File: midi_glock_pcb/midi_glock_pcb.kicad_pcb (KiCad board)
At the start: 2 copper layers, 7 parts, among them U11 ESP32-WROVER-E-N4R8, U12 DRV8860_PWPR, U13 DRV8860_PWPR, U14 DRV8860_PWPR, U15 DRV8860_PWPR, U6 TPS54302, U9 AMS1117-3.3

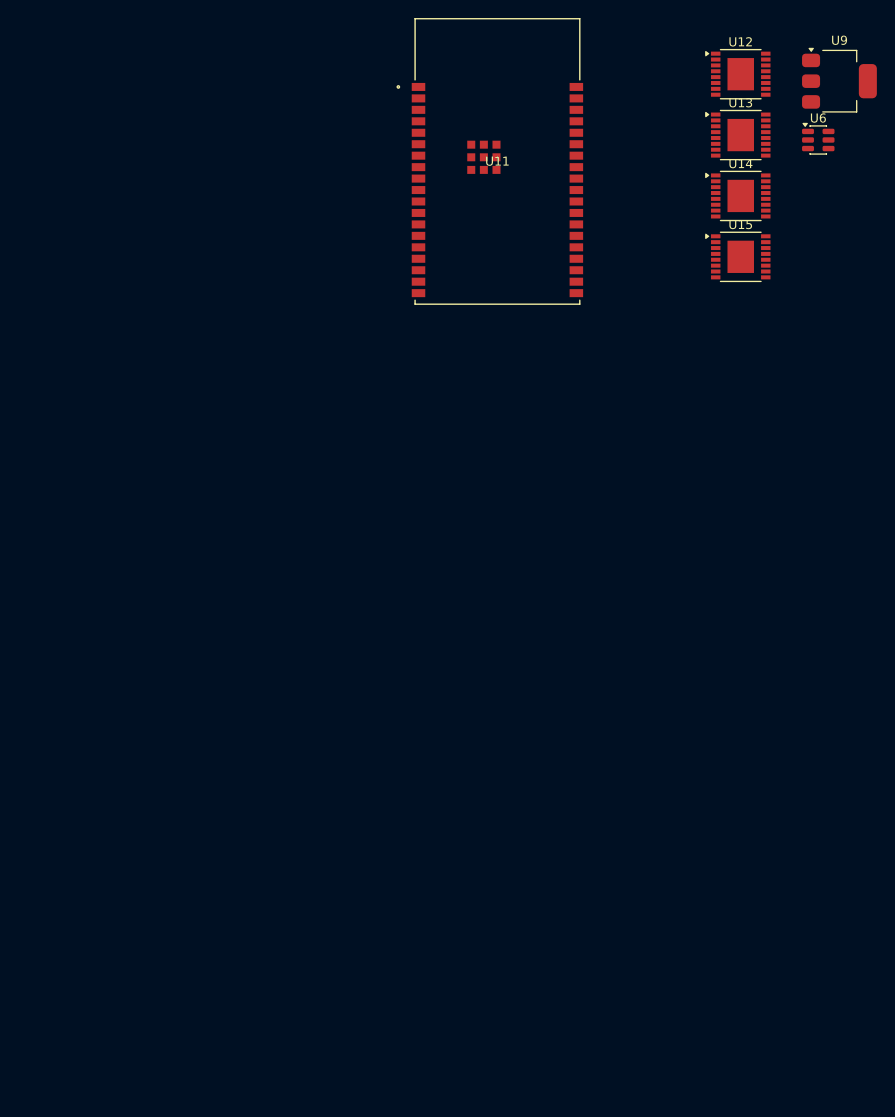
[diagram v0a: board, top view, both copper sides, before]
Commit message: pcb almost complete
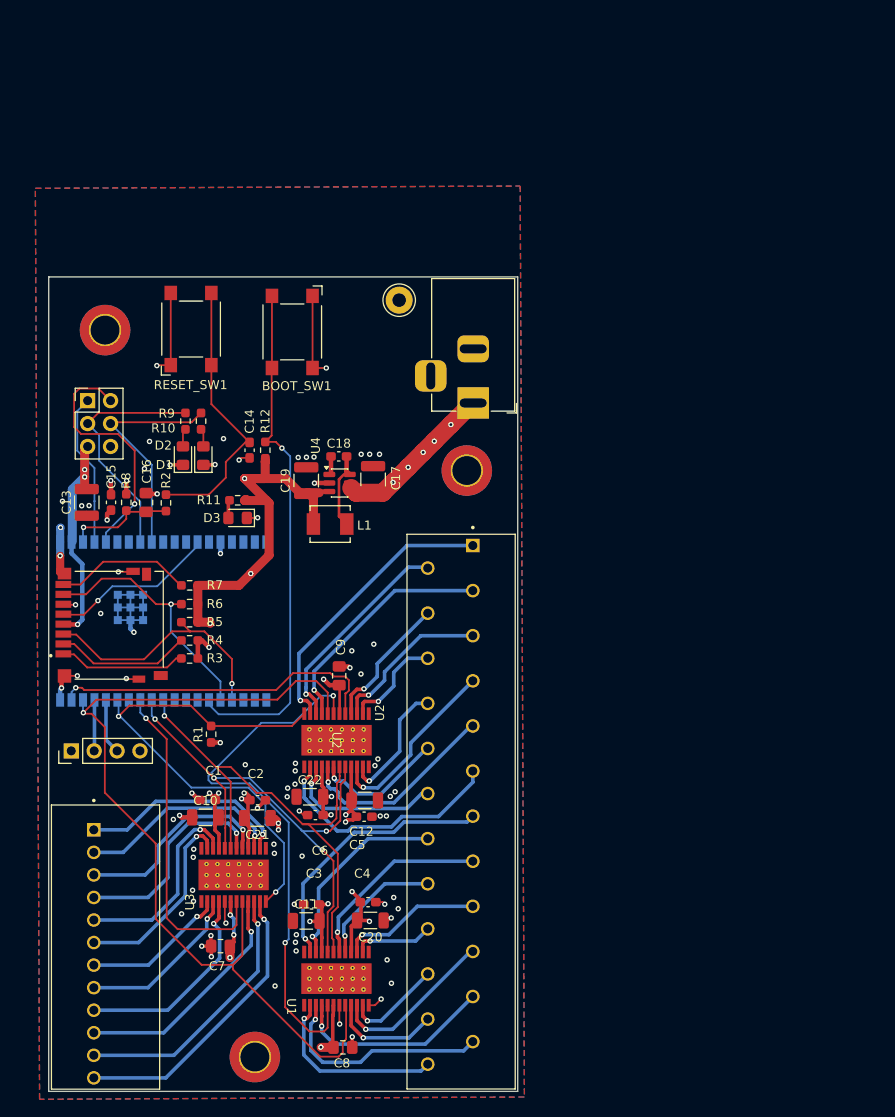
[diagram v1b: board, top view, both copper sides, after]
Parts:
- removed U12, U13, U14, U15: DRV8860_PWPR, Package_SO:TSSOP-16-1EP_4.4x5mm_P0.65mm
- removed U6: TPS54302, Package_TO_SOT_SMD:SOT-23-6
- removed U9: AMS1117-3.3, Package_TO_SOT_SMD:SOT-223-3_TabPin2
- added BOOT_SW1: SW_Push, Button_Switch_SMD:SW_SPST_Omron_B3FS-100xP, F.Cu at (75.0, 70.8)
- added C1: 0.1uF, Capacitor_SMD:C_0603_1608Metric_Pad1.08x0.95mm_HandSolder, F.Cu at (65.6, 122.7)
- added C10: 10uF, Capacitor_SMD:C_1206_3216Metric, F.Cu at (65.4, 124.6)
- added C11: 10uF, Capacitor_SMD:C_1206_3216Metric, F.Cu at (76.5, 136.1)
- added C12: 10uF, Capacitor_SMD:C_1206_3216Metric, F.Cu at (83.0, 122.7)
- added C13: 22uF, Capacitor_SMD:C_1210_3225Metric, F.Cu at (52.2, 89.7)
- added C14: 0.1uF, Capacitor_SMD:C_0603_1608Metric_Pad1.08x0.95mm_HandSolder, F.Cu at (70.3, 83.9)
- added C15: 0.1uF, Capacitor_SMD:C_0603_1608Metric_Pad1.08x0.95mm_HandSolder, F.Cu at (54.9, 89.7)
- added C16: 4.7uF, Capacitor_SMD:C_0805_2012Metric_Pad1.18x1.45mm_HandSolder, F.Cu at (58.8, 89.7)
- added C17: 22uf, Capacitor_SMD:C_1210_3225Metric, F.Cu at (84.0, 87.2)
- added C18: 100nf, Capacitor_SMD:C_0603_1608Metric_Pad1.08x0.95mm_HandSolder, F.Cu at (80.2, 84.6)
- added C19: 22uf, Capacitor_SMD:C_1210_3225Metric, F.Cu at (76.5, 87.3)
- added C2: 0.1uF, Capacitor_SMD:C_0603_1608Metric_Pad1.08x0.95mm_HandSolder, F.Cu at (71.2, 122.7)
- added C20: 10uF, Capacitor_SMD:C_1206_3216Metric, F.Cu at (83.7, 136.1)
- added C21: 10uF, Capacitor_SMD:C_1206_3216Metric, F.Cu at (71.1, 124.7)
- added C22: 10uF, Capacitor_SMD:C_1206_3216Metric, F.Cu at (77.0, 122.3)
- added C3: 0.1uF, Capacitor_SMD:C_0603_1608Metric_Pad1.08x0.95mm_HandSolder, F.Cu at (77.1, 134.3)
- added C4: 0.1uF, Capacitor_SMD:C_0603_1608Metric_Pad1.08x0.95mm_HandSolder, F.Cu at (83.4, 134.0)
- added C5: 0.1uF, Capacitor_SMD:C_0603_1608Metric_Pad1.08x0.95mm_HandSolder, F.Cu at (83.0, 124.5)
- added C6: 0.1uF, Capacitor_SMD:C_0603_1608Metric_Pad1.08x0.95mm_HandSolder, F.Cu at (77.6, 124.4)
- added C7: 10uF, Capacitor_SMD:C_0805_2012Metric_Pad1.18x1.45mm_HandSolder, F.Cu at (67.0, 138.9)
- added C8: 10uF, Capacitor_SMD:C_0805_2012Metric_Pad1.18x1.45mm_HandSolder, F.Cu at (80.6, 150.1)
- added C9: 10uF, Capacitor_SMD:C_0805_2012Metric_Pad1.18x1.45mm_HandSolder, F.Cu at (80.2, 108.9)
- added D1: LED2, LED_SMD:LED_0805_2012Metric_Pad1.15x1.40mm_HandSolder, F.Cu at (65.1, 84.5)
- added D2: LED1, LED_SMD:LED_0805_2012Metric_Pad1.15x1.40mm_HandSolder, F.Cu at (62.9, 84.5)
- added D3: PWR_LED, LED_SMD:LED_0805_2012Metric_Pad1.15x1.40mm_HandSolder, F.Cu at (68.9, 91.4)
- added J1: Conn_01x12_Pin, midi_glock_footprints:PHOENIX_1989845, F.Cu at (48.3, 123.2)
- added J2: Conn_01x24_Pin, midi_glock_footprints:PHOENIX_1990232, F.Cu at (99.7, 154.7)
- added J3: Jack-DC, Connector_BarrelJack:BarrelJack_Horizontal, F.Cu at (95.1, 78.7)
- added J4: Conn_01x06_Pin, Connector_PinHeader_2.54mm:PinHeader_2x03_P2.54mm_Vertical, F.Cu at (52.3, 78.4)
- added J5: solenoid_return, Connector_Pin:Pin_D1.3mm_L11.0mm_LooseFit, F.Cu at (86.9, 67.3)
- added J6: DM3D-SF, midi_glock_footprints:HRS_DM3D-SF, F.Cu at (49.6, 103.3)
- added J7: Conn_01x04_Pin, Connector_PinHeader_2.54mm:PinHeader_1x04_P2.54mm_Vertical, F.Cu at (50.5, 117.2)
- added L1: 4.7uH, midi_glock_footprints:IND_SRP4020TA-4R7M, F.Cu at (79.2, 92.1)
- added R1: 10k, Resistor_SMD:R_0603_1608Metric_Pad0.98x0.95mm_HandSolder, F.Cu at (66.0, 115.4)
- added R10: 1k, Resistor_SMD:R_0603_1608Metric_Pad0.98x0.95mm_HandSolder, F.Cu at (63.2, 80.7)
- added R11: 1k, Resistor_SMD:R_0603_1608Metric_Pad0.98x0.95mm_HandSolder, F.Cu at (69.0, 89.5)
- added R12: 10k, Resistor_SMD:R_0603_1608Metric_Pad0.98x0.95mm_HandSolder, F.Cu at (72.0, 83.9)
- added R2: 0, Resistor_SMD:R_0603_1608Metric_Pad0.98x0.95mm_HandSolder, F.Cu at (61.0, 89.8)
- added R3: 47k, Resistor_SMD:R_0603_1608Metric_Pad0.98x0.95mm_HandSolder, F.Cu at (63.6, 107.0)
- added R4: 47k, Resistor_SMD:R_0603_1608Metric_Pad0.98x0.95mm_HandSolder, F.Cu at (63.6, 105.0)
- added R5: 47k, Resistor_SMD:R_0603_1608Metric_Pad0.98x0.95mm_HandSolder, F.Cu at (63.6, 103.0)
- added R6: 47k, Resistor_SMD:R_0603_1608Metric_Pad0.98x0.95mm_HandSolder, F.Cu at (63.6, 101.0)
- added R7: 47k, Resistor_SMD:R_0603_1608Metric_Pad0.98x0.95mm_HandSolder, F.Cu at (63.6, 98.9)
- added R8: 10k, Resistor_SMD:R_0603_1608Metric_Pad0.98x0.95mm_HandSolder, F.Cu at (56.6, 89.7)
- added R9: 1k, Resistor_SMD:R_0603_1608Metric_Pad0.98x0.95mm_HandSolder, F.Cu at (64.9, 80.7)
- added REF**: MountingHole_3.2mm_M3_DIN965_Pad_TopBottom, MountingHole:MountingHole_3.2mm_M3_DIN965_Pad_TopBottom, F.Cu at (54.2, 70.6)
- added REF**: MountingHole_3.2mm_M3_DIN965_Pad_TopBottom, MountingHole:MountingHole_3.2mm_M3_DIN965_Pad_TopBottom, F.Cu at (94.4, 86.2)
- added REF**: MountingHole_3.2mm_M3_DIN965_Pad_TopBottom, MountingHole:MountingHole_3.2mm_M3_DIN965_Pad_TopBottom, F.Cu at (70.9, 151.2)
- added RESET_SW1: SW_Push, Button_Switch_SMD:SW_SPST_Omron_B3FS-100xP, F.Cu at (63.8, 70.5)
- added U1: DRV8912QPWPRQ1, midi_glock_footprints:PWP0024N_N, F.Cu at (79.9, 142.5)
- added U2: DRV8912QPWPRQ1, midi_glock_footprints:PWP0024N_N, F.Cu at (79.9, 116.1)
- added U3: DRV8912QPWPRQ1, midi_glock_footprints:PWP0024N_N, F.Cu at (68.5, 131.0)
- added U4: LMR50410Y3FQDBVRQ1, Package_TO_SOT_SMD:SOT-23-6, F.Cu at (80.2, 87.5)
- U5: renamed from U11; moved to B.Cu
- moved U5 64.9 mm to (57.5, 102.9), turned to -90 degrees
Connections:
- U5 pad 13: unconnected-(U11-IO14-Pad13) -> /SDIO_CLK
- U5 pad 15: unconnected-(U11-GND-Pad15) -> GND
- U5 pad 23: unconnected-(U11-IO15-Pad23) -> /SDIO_CMD
- U5 pad 24: unconnected-(U11-IO2-Pad24) -> /SDIO_D0
- U5 pad 25: unconnected-(U11-IO0-Pad25) -> Net-(U5-IO0)
- U5 pad 29: unconnected-(U11-IO5-Pad29) -> /SPI_CS
- U5 pad 30: unconnected-(U11-IO18-Pad30) -> /SPI_SCLK
- U5 pad 31: unconnected-(U11-IO19-Pad31) -> /SPI_MISO
- U5 pad 33: unconnected-(U11-IO21-Pad33) -> /DRV_nFAULT
- U5 pad 34: unconnected-(U11-RXD0-Pad34) -> Net-(J7-Pin_3)
- U5 pad 35: unconnected-(U11-TXD0-Pad35) -> Net-(J7-Pin_2)
- U5 pad 36: unconnected-(U11-IO22-Pad36) -> /DRV_nSLEEP
- U5 pad 37: unconnected-(U11-IO23-Pad37) -> /SPI_MOSI
- U5 pad 4: unconnected-(U11-SENSOR_VP-Pad4) -> /IO_36
- U5 pad 5: unconnected-(U11-SENSOR_VN-Pad5) -> /IO_39
- U5 pad 8: unconnected-(U11-IO32-Pad8) -> /IO_32
- U5 pad 9: unconnected-(U11-IO33-Pad9) -> /IO_33
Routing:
- net +3.3V: track 0.00 -> 211.5 mm, vias 0 -> 15
- net /DRV_nSLEEP: track 0.00 -> 99.9 mm, vias 0 -> 1
- net GND: track 0.00 -> 96.1 mm, vias 0 -> 77
- net /DRV_nFAULT: track 0.00 -> 80.5 mm, vias 0 -> 3
- net +24V: track 0.00 -> 68.0 mm, vias 0 -> 17
- net Net-(U1-SDI): track 0.00 -> 60.2 mm, vias 0 -> 2
- net /SPI_SCLK: track 0.00 -> 59.6 mm, vias 0 -> 4
- net /SPI_CS: track 0.00 -> 59.1 mm, vias 0 -> 1
- net Net-(U5-IO0): track 0.00 -> 57.8 mm, vias 0 -> 1
- net /SPI_MISO: track 0.00 -> 37.1 mm, vias 0 -> 1
- net /SPI_MOSI: track 0.00 -> 36.9 mm, vias 0 -> 1
- net /S9: track 0.00 -> 32.5 mm, vias 0 -> 1
- net /S33: track 0.00 -> 31.8 mm, vias 0 -> 1
- net Net-(C14-Pad2): track 0.00 -> 31.0 mm
- net /S7: track 0.00 -> 30.0 mm, vias 0 -> 1
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- added copper zone on In2.Cu, net +24V
- added copper zone on B.Cu, net GND
- added copper zone on F.Cu, net GND
- added copper zone on In1.Cu, net GND
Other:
- board outline added: 52 x 90.3 mm
- copper layers 2 -> 4

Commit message: more pcb updates
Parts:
- moved C17 0.13 mm to (84.0, 87.3)
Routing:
- net +3.3V: track 211.5 -> 208.3 mm
- net GND: track 96.1 -> 93.5 mm
- net /S13: track 21.5 -> 22.3 mm
- net /S14: track 14.3 -> 13.7 mm

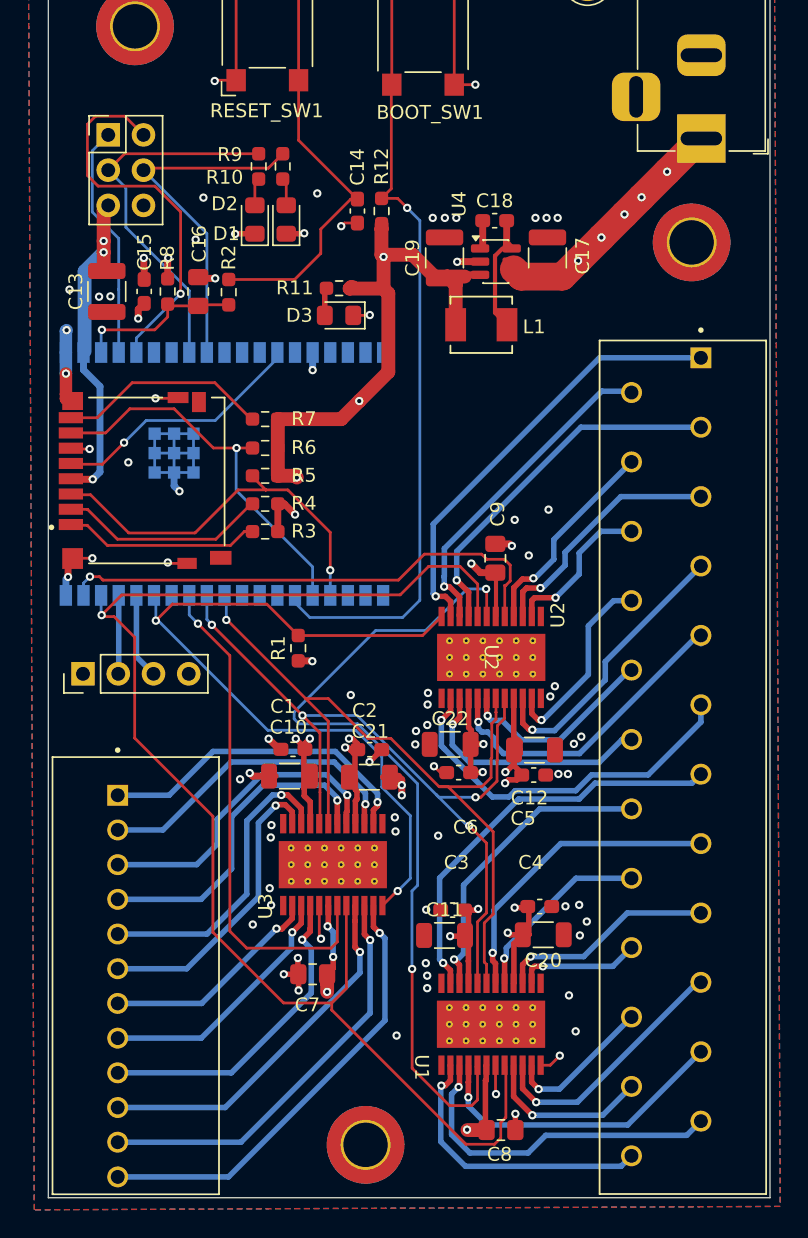
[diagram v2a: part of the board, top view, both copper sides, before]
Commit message: fixed issues with drv vias on footprint causing drc errors
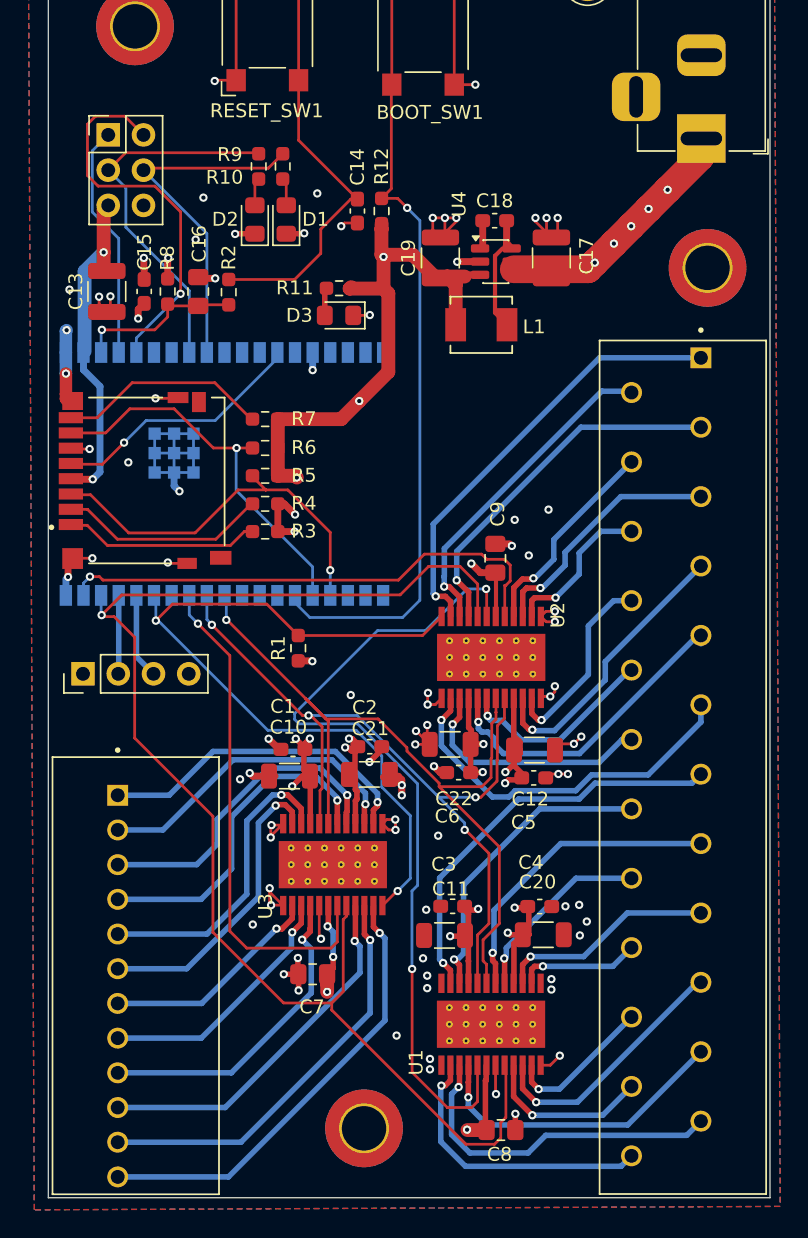
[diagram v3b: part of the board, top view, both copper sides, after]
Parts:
- moved REF** 2.16 mm to (95.5, 88.0)
- moved REF** 1.20 mm to (70.8, 150.0)
- moved C19 0.30 mm to (76.2, 87.3)
- moved C17 0.28 mm to (84.2, 87.3)
- moved C3 0.27 mm to (77.1, 134.0)
- moved C2 0.22 mm to (71.2, 122.5)
- moved C5 0.20 mm to (83.0, 124.8)
- moved C21 0.20 mm to (71.1, 124.5)
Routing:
- net GND: track 93.5 -> 128.6 mm, vias 77 -> 81
- net +24V: track 68.0 -> 66.3 mm, vias 17 -> 18
- net +3.3V: track 208.3 -> 209.9 mm
- net /SPI_SCLK: track 59.6 -> 58.5 mm
- net Net-(D3-A): track 2.64 -> 1.83 mm
- net /SPI_CS: track 59.1 -> 58.3 mm
- net Net-(U5-EN): track 12.6 -> 11.9 mm
- net Net-(J7-Pin_3): track 6.16 -> 5.52 mm
- net /SPI_MISO: track 37.1 -> 36.5 mm
- net Net-(U5-IO0): track 57.8 -> 57.2 mm
- net /S1: track 23.7 -> 24.2 mm

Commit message: pcb v1 finished
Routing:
- net +24V: track 66.3 -> 67.8 mm, vias 18 -> 19
- net +3.3V: track 209.9 -> 209.0 mm

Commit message: added test points
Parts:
- added TP1: MOSI, TestPoint:TestPoint_Pad_D1.0mm, F.Cu at (75.1, 108.6)
- added TP2: MISO, TestPoint:TestPoint_Pad_D1.0mm, F.Cu at (61.1, 120.2)
- added TP3: CS, TestPoint:TestPoint_Pad_D1.0mm, F.Cu at (62.9, 115.1)
- added TP4: CLK, TestPoint:TestPoint_Pad_D1.0mm, F.Cu at (63.6, 117.8)
- BOOT_SW1: value SW_Push -> BOOT
- RESET_SW1: value SW_Push -> RESET
